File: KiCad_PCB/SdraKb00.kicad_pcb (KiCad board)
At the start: 2 copper layers, 3.6 x 3.3 mm, 75 parts, among them J1 AVR-ISP-6, SW00 SW_Push_45deg, SW01 SW_Push_45deg, SW02 SW_Push_45deg, SW03 RotaryEncoder_Switch, SW10 SW_Push_45deg, SW11 SW_Push_45deg, SW12 SW_Push_45deg, SW13 SW_Push_45deg, SW20 SW_Push_45deg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

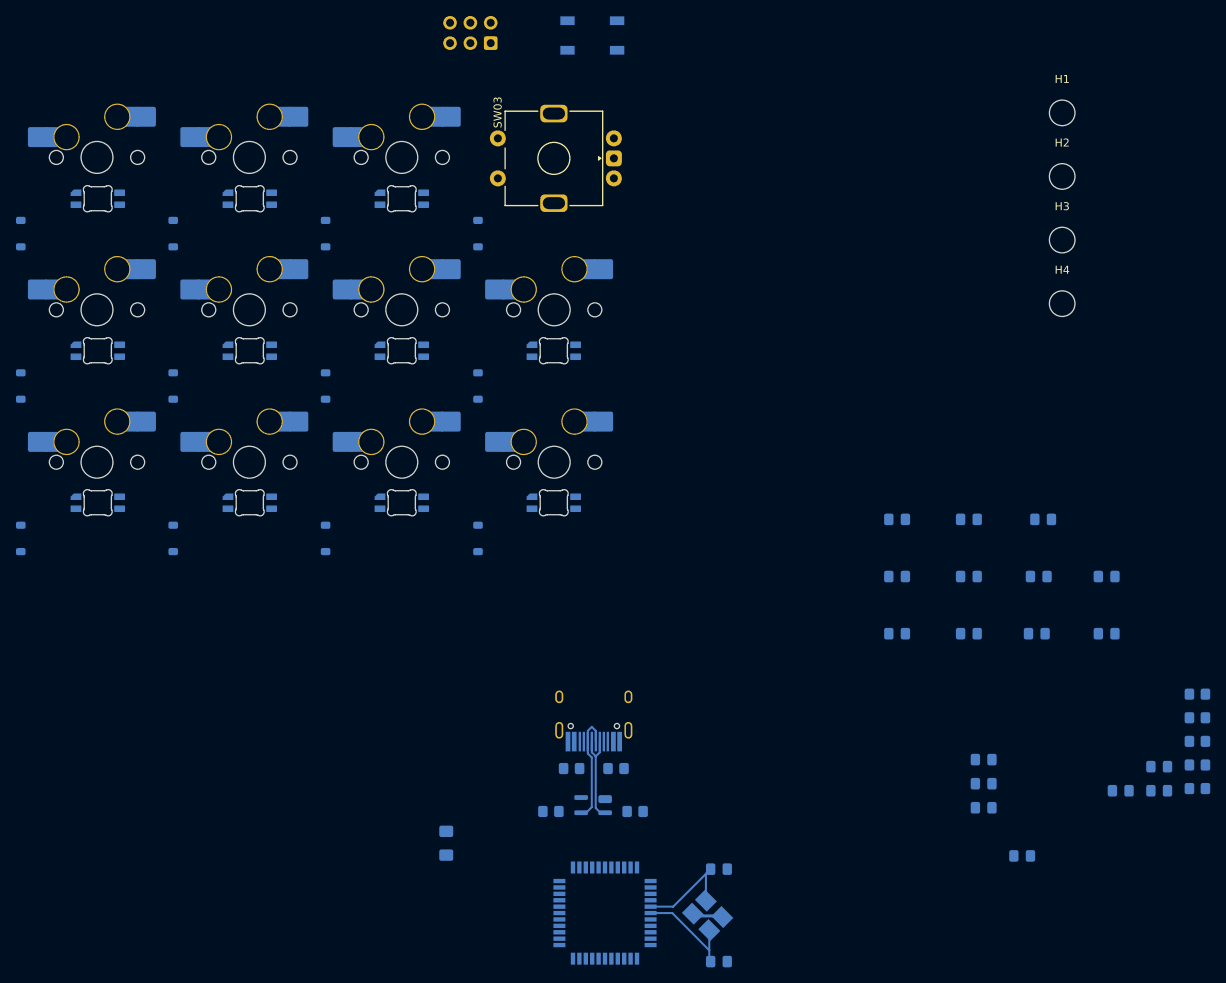
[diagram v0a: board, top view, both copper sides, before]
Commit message: Placing all components before routing.
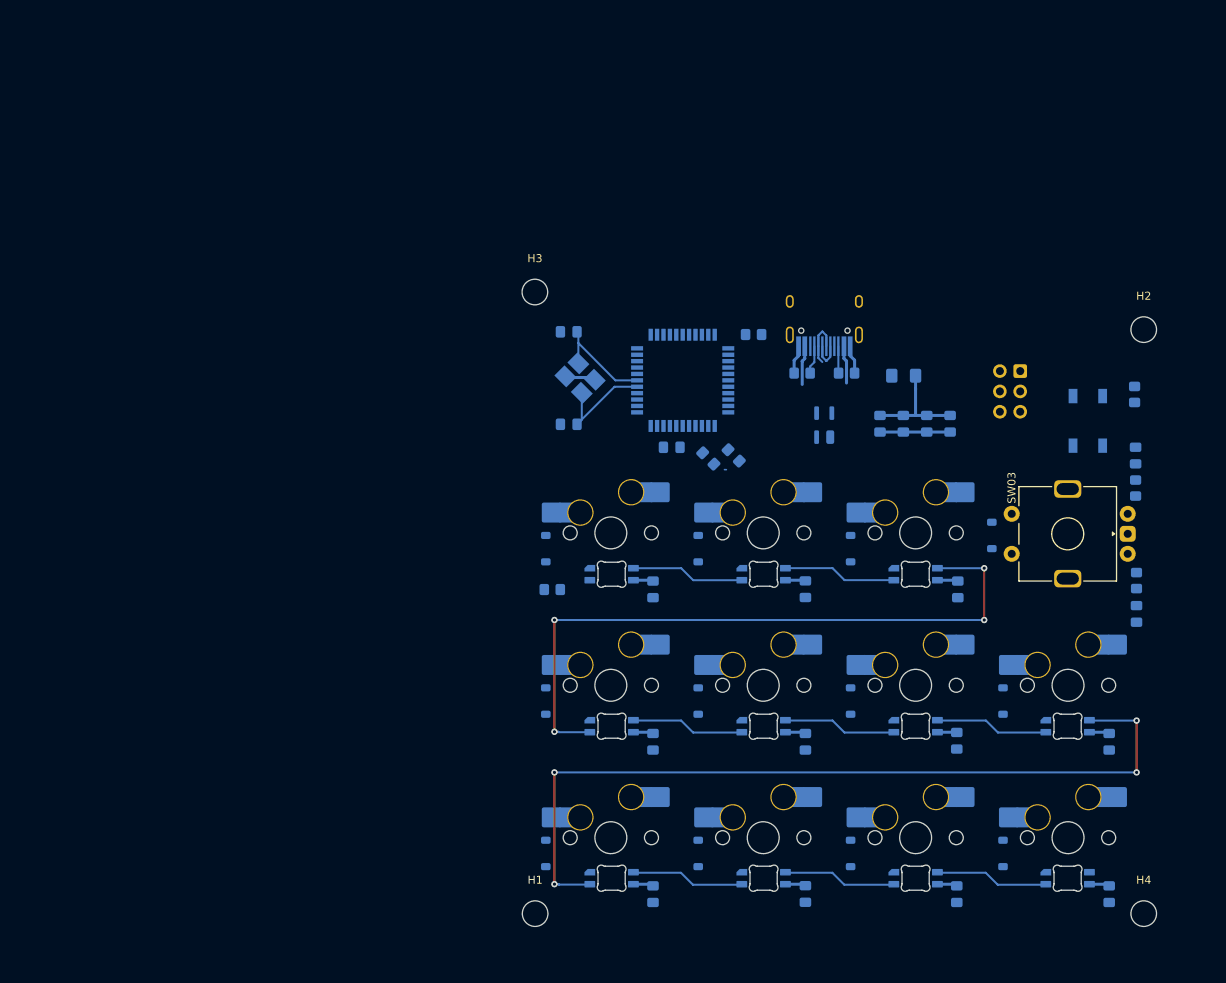
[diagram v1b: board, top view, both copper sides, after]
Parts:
- moved H1 119.8 mm to (105.6, 140.6)
- moved F1 81.8 mm to (151.6, 73.3), turned to 0 degrees
- moved R1 81.7 mm to (107.7, 100.1), turned to 0 degrees
- moved C20 80.9 mm to (109.8, 67.8), turned to 180 degrees
- moved SW00 79.5 mm to (115.0, 93.0)
- moved SW10 79.5 mm to (115.0, 112.0)
- moved SW13 79.5 mm to (172.2, 112.0)
- moved SW20 79.5 mm to (115.0, 131.1)
- moved SW23 79.5 mm to (172.2, 131.1)
- moved RGB00 79.5 mm to (115.1, 98.1)
- moved RGB01 79.5 mm to (134.1, 98.1)
- moved RGB02 79.5 mm to (153.1, 98.1)
- moved RGB20 79.5 mm to (115.1, 136.1)
- moved RGB21 79.5 mm to (134.1, 136.1)
- moved RGB22 79.5 mm to (153.1, 136.1)
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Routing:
- net Net-(RGB13-DOUT): track 0.00 -> 103.5 mm, vias 0 -> 4
- net Net-(RGB02-DOUT): track 0.00 -> 84.5 mm, vias 0 -> 4
- net +5V: track 0.00 -> 41.5 mm
- net GND: track 3.85 -> 19.8 mm
- net Net-(RGB21-DOUT): track 0.00 -> 14.2 mm
- net Net-(RGB11-DOUT): track 0.00 -> 14.2 mm
- net Net-(RGB01-DOUT): track 0.00 -> 14.2 mm
- net Net-(RGB20-DOUT): track 0.00 -> 14.2 mm
- net Net-(RGB10-DOUT): track 0.00 -> 14.2 mm
- net Net-(RGB00-DOUT): track 0.00 -> 14.2 mm
- net Net-(RGB22-DOUT): track 0.00 -> 14.2 mm
- net Net-(RGB12-DOUT): track 0.00 -> 14.2 mm
- net VCC: track 0.00 -> 9.65 mm
- net Net-(U2-IO2): track 14.1 -> 6.28 mm
- net Net-(U2-IO1): track 12.0 -> 4.37 mm
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
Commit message: More wiring.
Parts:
- J1: footprint Connector_IDC:IDC-Header_2x03_P2.54mm_Vertical -> Connector_PinHeader_2.00mm:PinHeader_1x06_P2.00mm_Vertical
- moved H3 4.70 mm to (105.5, 67.6)
- moved J1 3.14 mm to (164.7, 70.0)
- moved SW_rst1 1.27 mm to (173.5, 78.5)
- moved C19 1.18 mm to (111.0, 79.4)
- moved Y1 1.18 mm to (112.4, 73.6)
- moved C20 1.18 mm to (111.0, 67.8)
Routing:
- net Row2: track 0.00 -> 58.8 mm
- net Row1: track 0.00 -> 58.7 mm
- net Row0: track 0.00 -> 57.4 mm
- net Col0: track 0.00 -> 39.4 mm, vias 0 -> 4
- net Col2: track 0.00 -> 39.4 mm, vias 0 -> 4
- net Col1: track 0.00 -> 39.4 mm, vias 0 -> 4
- net Col3: track 0.00 -> 38.7 mm, vias 0 -> 4
- net VCC: track 9.65 -> 15.9 mm, vias 0 -> 3
- net Net-(U1-~{HWB}/PE2): track 0.00 -> 5.32 mm
- net Net-(D00-A): track 0.00 -> 4.35 mm
- net Net-(D23-A): track 0.00 -> 3.18 mm
- net Net-(D22-A): track 0.00 -> 3.18 mm
- net Net-(D21-A): track 0.00 -> 3.18 mm
- net Net-(D20-A): track 0.00 -> 3.18 mm
- net Net-(D13-A): track 0.00 -> 3.18 mm
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
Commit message: More PCB routing.
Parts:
- moved R7 17.7 mm to (144.8, 81.3), turned to -90 degrees
- moved R6 11.5 mm to (141.7, 81.3), turned to -90 degrees
- moved SW_rst1 4.74 mm to (169.0, 76.8)
- moved J1 4.14 mm to (161.4, 67.4), turned to -90 degrees
- moved U2 2.65 mm to (143.2, 77.3), turned to 180 degrees
- moved R4 2.64 mm to (135.5, 68.5)
- moved U1 2.64 mm to (126.6, 74.2)
- moved C10 2.64 mm to (125.3, 82.5)
- moved C19 2.64 mm to (113.6, 79.7)
- moved C20 2.64 mm to (113.6, 68.1)
- moved Y1 2.64 mm to (115.0, 73.9)
- moved C15 2.02 mm to (150.7, 79.3)
- moved C18 2.02 mm to (159.5, 79.3)
- moved F1 2.02 mm to (153.7, 73.3)
- moved R8 2.02 mm to (146.5, 73.0)
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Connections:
- net Net-(U2-IO1) renamed DN
- net Net-(U2-IO2) renamed DP
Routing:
- net D+: track 0.00 -> 18.7 mm
- net D-: track 0.00 -> 18.5 mm
- net DN: track 4.37 -> 15.2 mm
- net DP: track 6.28 -> 15.3 mm
- net Net-(U1-UCAP): track 0.00 -> 2.81 mm

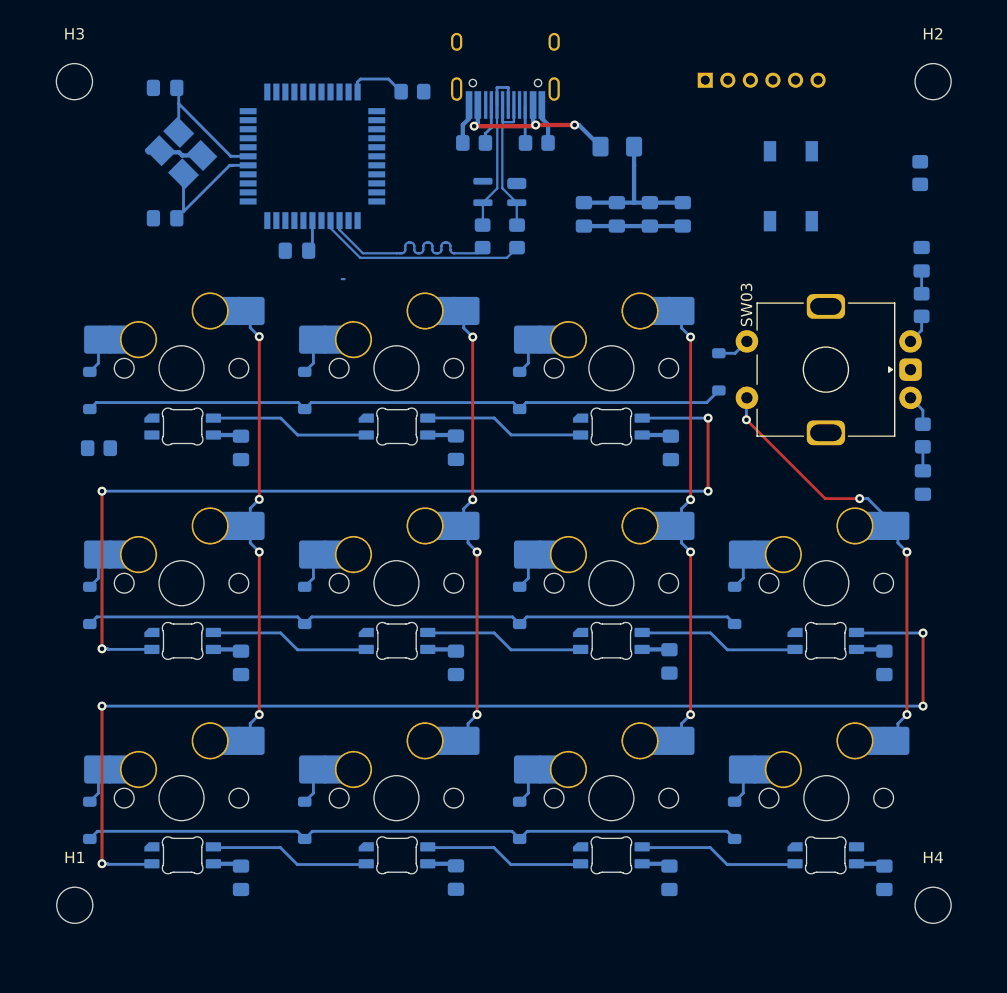
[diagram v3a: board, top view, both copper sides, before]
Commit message: Routing MCU powerlines, Crystal ground zone.
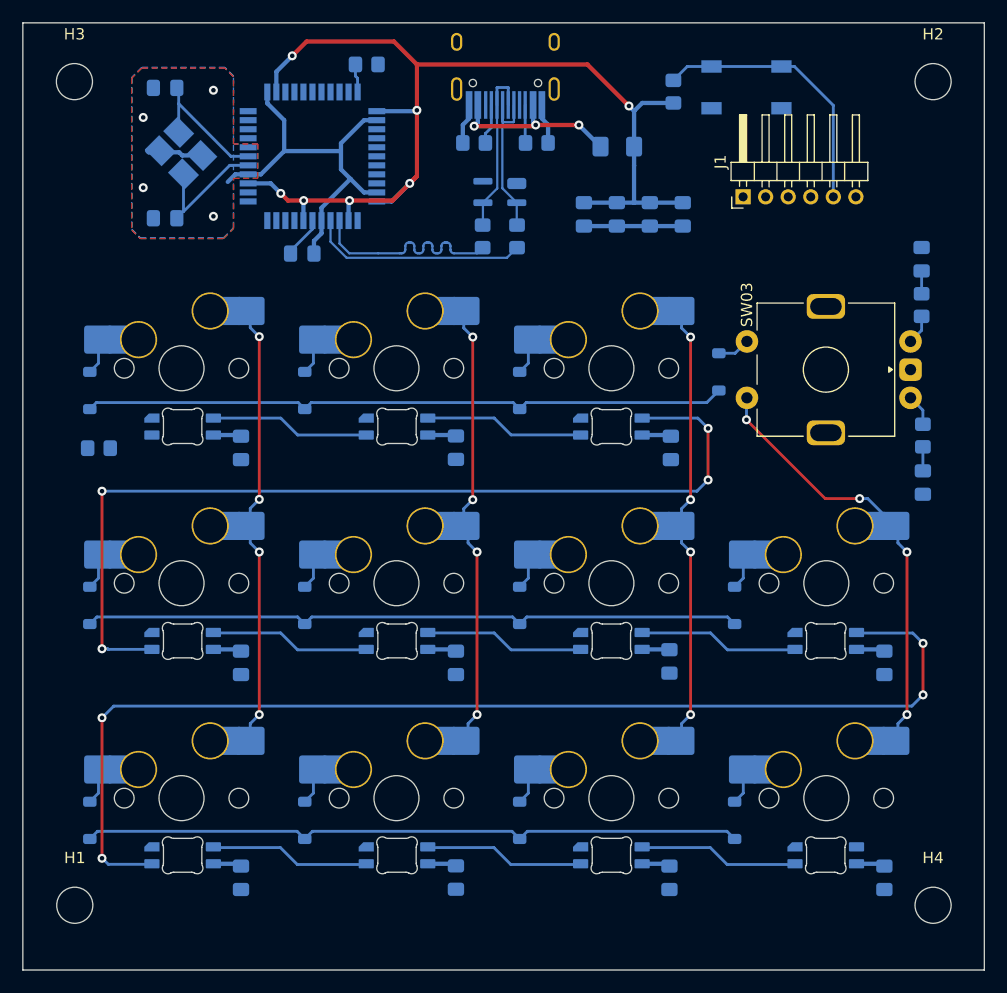
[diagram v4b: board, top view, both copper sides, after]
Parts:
- J1: footprint Connector_PinHeader_2.00mm:PinHeader_1x06_P2.00mm_Vertical -> Connector_PinHeader_2.00mm:PinHeader_1x06_P2.00mm_Horizontal; moved to F.Cu
- moved R5 23.0 mm to (158.6, 68.5), turned to 90 degrees
- moved J1 10.9 mm to (164.8, 77.8), turned to 90 degrees
- moved SW_rst1 9.61 mm to (165.1, 68.1), turned to 0 degrees
- moved R4 4.71 mm to (131.4, 66.0)
- moved C10 0.53 mm to (125.7, 82.8), turned to 0 degrees
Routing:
- net +5V: track 41.5 -> 123.5 mm, vias 0 -> 7
- net GND: track 19.8 -> 55.1 mm, vias 0 -> 4
- net RESET: track 0.00 -> 24.2 mm
- net Net-(U1-~{HWB}/PE2): track 5.32 -> 2.52 mm
- net Net-(RGB13-DOUT): track 103.5 -> 101.5 mm
- net Net-(RGB02-DOUT): track 84.5 -> 83.3 mm
- net Net-(U1-UCAP): track 2.81 -> 3.73 mm
- net D-: track 18.5 -> 19.2 mm
- net D+: track 18.7 -> 19.4 mm
- added copper zone on B.Cu, net (none)
- added copper zone on B.Cu, net GND
- added copper zone on F.Cu, net GND
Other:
- board size 3.6 x 3.3 mm -> 85.2 x 83.9 mm

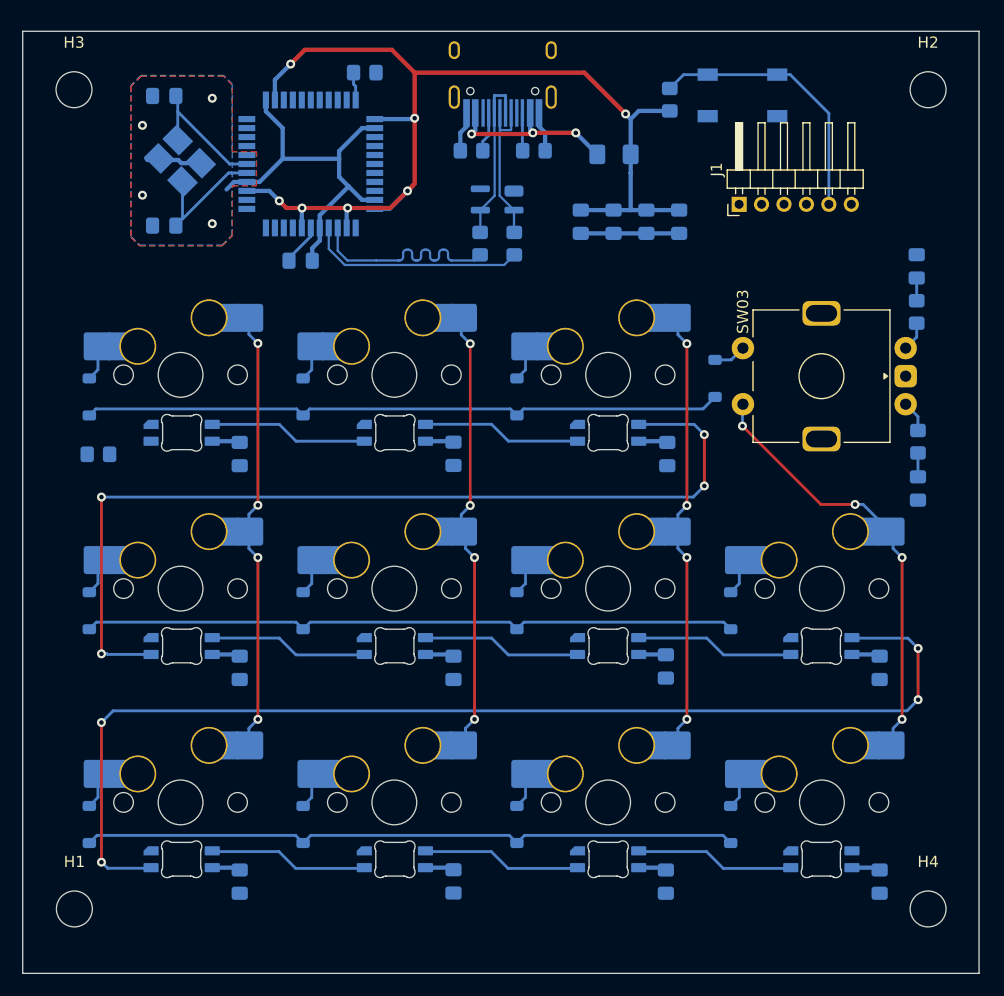
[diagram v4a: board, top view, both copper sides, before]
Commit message: Finish routing power.
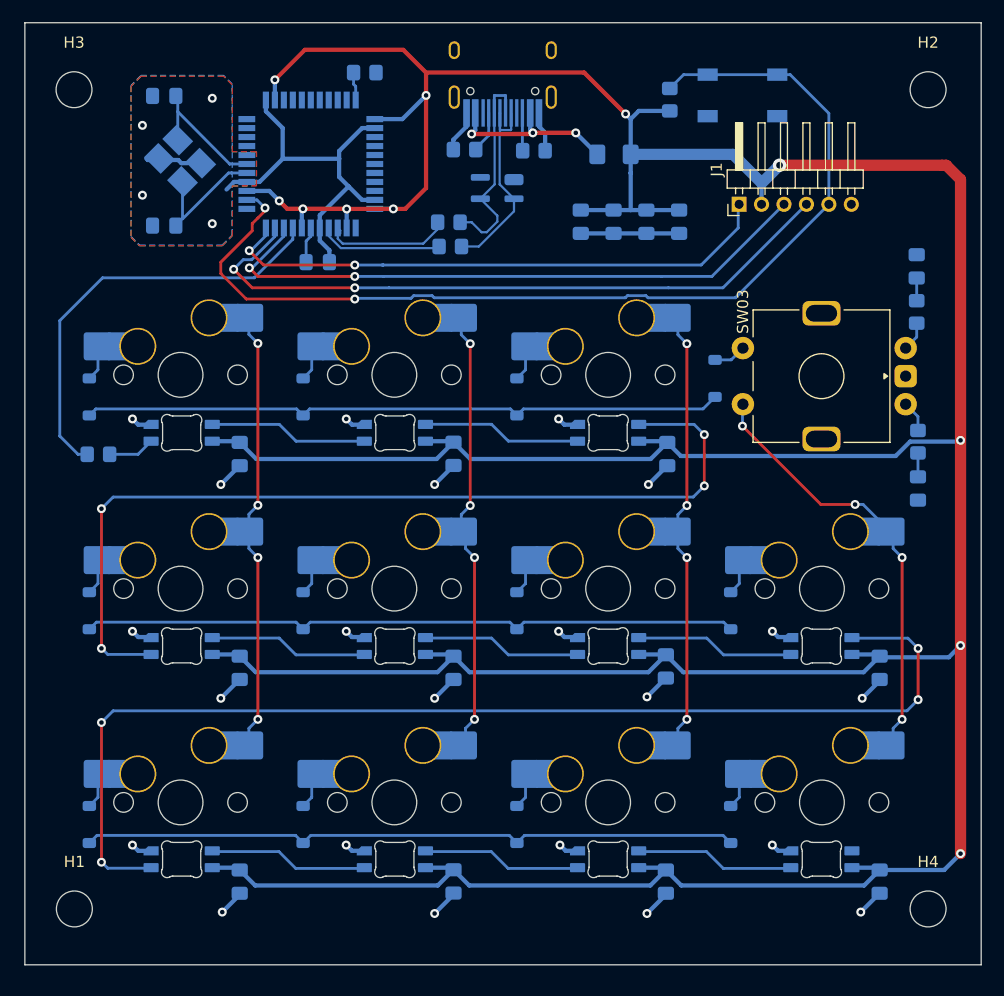
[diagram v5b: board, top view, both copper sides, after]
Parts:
- moved R7 5.71 mm to (139.1, 81.5), turned to 180 degrees
- moved R6 3.37 mm to (138.9, 79.4), turned to 180 degrees
- moved C10 1.53 mm to (127.3, 82.9)
- moved U2 1.02 mm to (143.2, 76.3)
- moved R9 0.63 mm to (140.3, 72.9)
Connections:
- U1 pad 18: Col3 -> unconnected-(U1-PD0-Pad18)
- U1 pad 19: Col2 -> unconnected-(U1-PD1-Pad19)
- U1 pad 20: Col1 -> unconnected-(U1-PD2-Pad20)
- U1 pad 21: Col0 -> unconnected-(U1-PD3-Pad21)
- U1 pad 38: unconnected-(U1-PF5-Pad38) -> Col3
- U1 pad 39: unconnected-(U1-PF4-Pad39) -> Col2
- U1 pad 40: unconnected-(U1-PF1-Pad40) -> Col1
- U1 pad 41: RGB_CHAIN -> Col0
- U1 pad 8: unconnected-(U1-PB0-Pad8) -> RGB_CHAIN
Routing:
- net +5V: track 123.5 -> 421.9 mm, vias 7 -> 11
- net RESET: track 24.2 -> 93.0 mm, vias 0 -> 2
- net MOSI: track 0.00 -> 60.4 mm, vias 0 -> 2
- net SCK: track 0.00 -> 55.6 mm, vias 0 -> 2
- net MISO: track 0.00 -> 50.5 mm, vias 0 -> 2
- net GND: track 55.1 -> 101.9 mm, vias 4 -> 26
- net RGB_CHAIN: track 0.00 -> 38.2 mm
- net D+: track 19.4 -> 11.1 mm
- net D-: track 19.2 -> 11.8 mm
- net Net-(RGB00-DIN): track 0.00 -> 4.17 mm
- net DN: track 15.2 -> 19.3 mm
- net DP: track 15.3 -> 19.0 mm
- net Net-(RGB02-DOUT): track 83.3 -> 82.5 mm
- net Col1: track 39.4 -> 40.0 mm
- net Net-(U1-UCAP): track 3.73 -> 3.22 mm
